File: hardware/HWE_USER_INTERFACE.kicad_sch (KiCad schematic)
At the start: 0 parts

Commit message: feat: Created Button I2C Interfaces
For now, all we are using is generic 1x5 Connectors following the DFR Robot's RGB Button pinout https://wiki.dfrobot.com/SKU_DFR0991_Gravity_I2C_RGB_LED_Button_Module#target_9
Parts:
- added J4: BTN_PLAY, symbol Connector_Generic:Conn_01x05
- added J5: BTN_REC, symbol Connector_Generic:Conn_01x05
- added J6: BTN_STOP, symbol Connector_Generic:Conn_01x05
- added J7: BTN_QUANTISE, symbol Connector_Generic:Conn_01x05
- added J8: BTN_OVERDUB, symbol Connector_Generic:Conn_01x05
- added J9: BTN_METRONOME, symbol Connector_Generic:Conn_01x05
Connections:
- new net +5V: J4.1 (Pin_1), J5.1 (Pin_1), J6.1 (Pin_1), J7.1 (Pin_1), J8.1 (Pin_1), J9.1 (Pin_1)
- new net BTN_METRONOME_INT: J9.5 (Pin_5)
- new net BTN_OVERDUB_INT: J8.5 (Pin_5)
- new net BTN_PLAY_INT: J4.5 (Pin_5)
- new net BTN_QUANTISE_INT: J7.5 (Pin_5)
- new net BTN_REC_INT: J5.5 (Pin_5)
- new net BTN_STOP_INT: J6.5 (Pin_5)
- new net GND: J4.2 (Pin_2), J5.2 (Pin_2), J6.2 (Pin_2), J7.2 (Pin_2), J8.2 (Pin_2), J9.2 (Pin_2)
- new net SCL: J4.3 (Pin_3)
- new net SDA: J4.4 (Pin_4), J5.4 (Pin_4), J6.4 (Pin_4), J7.4 (Pin_4), J8.4 (Pin_4), J9.4 (Pin_4)

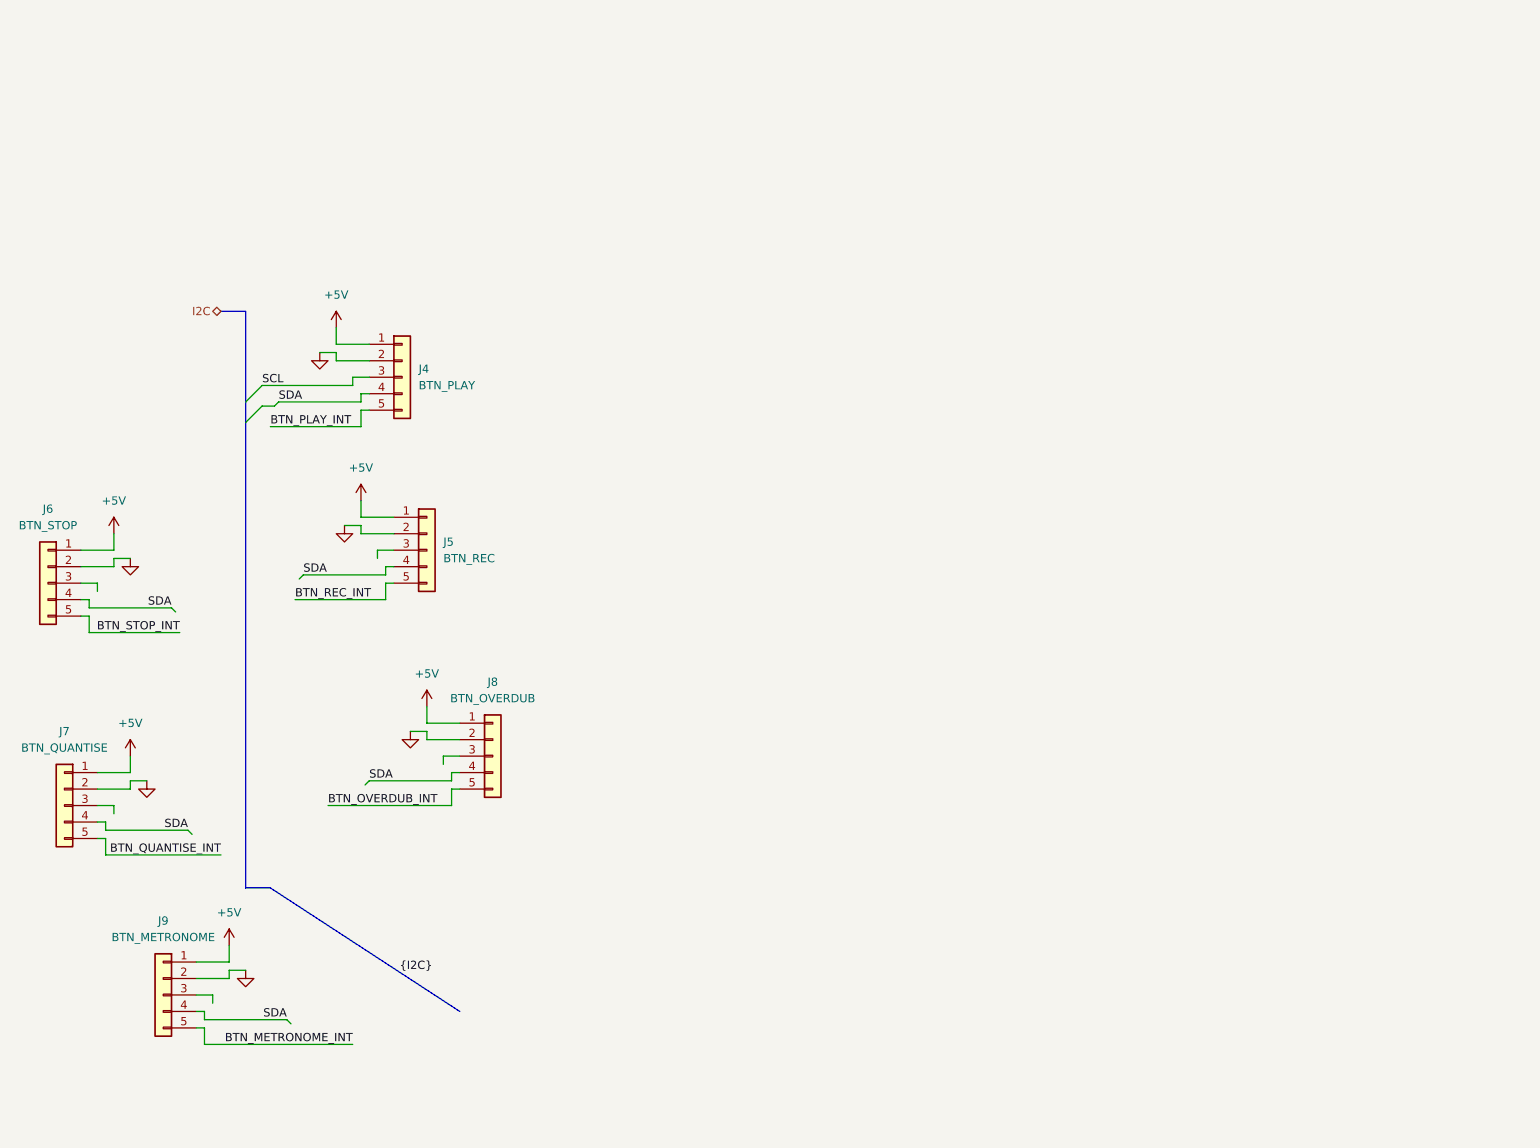
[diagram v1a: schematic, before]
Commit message: feat: Added Volume and Inf Scroll Encoders
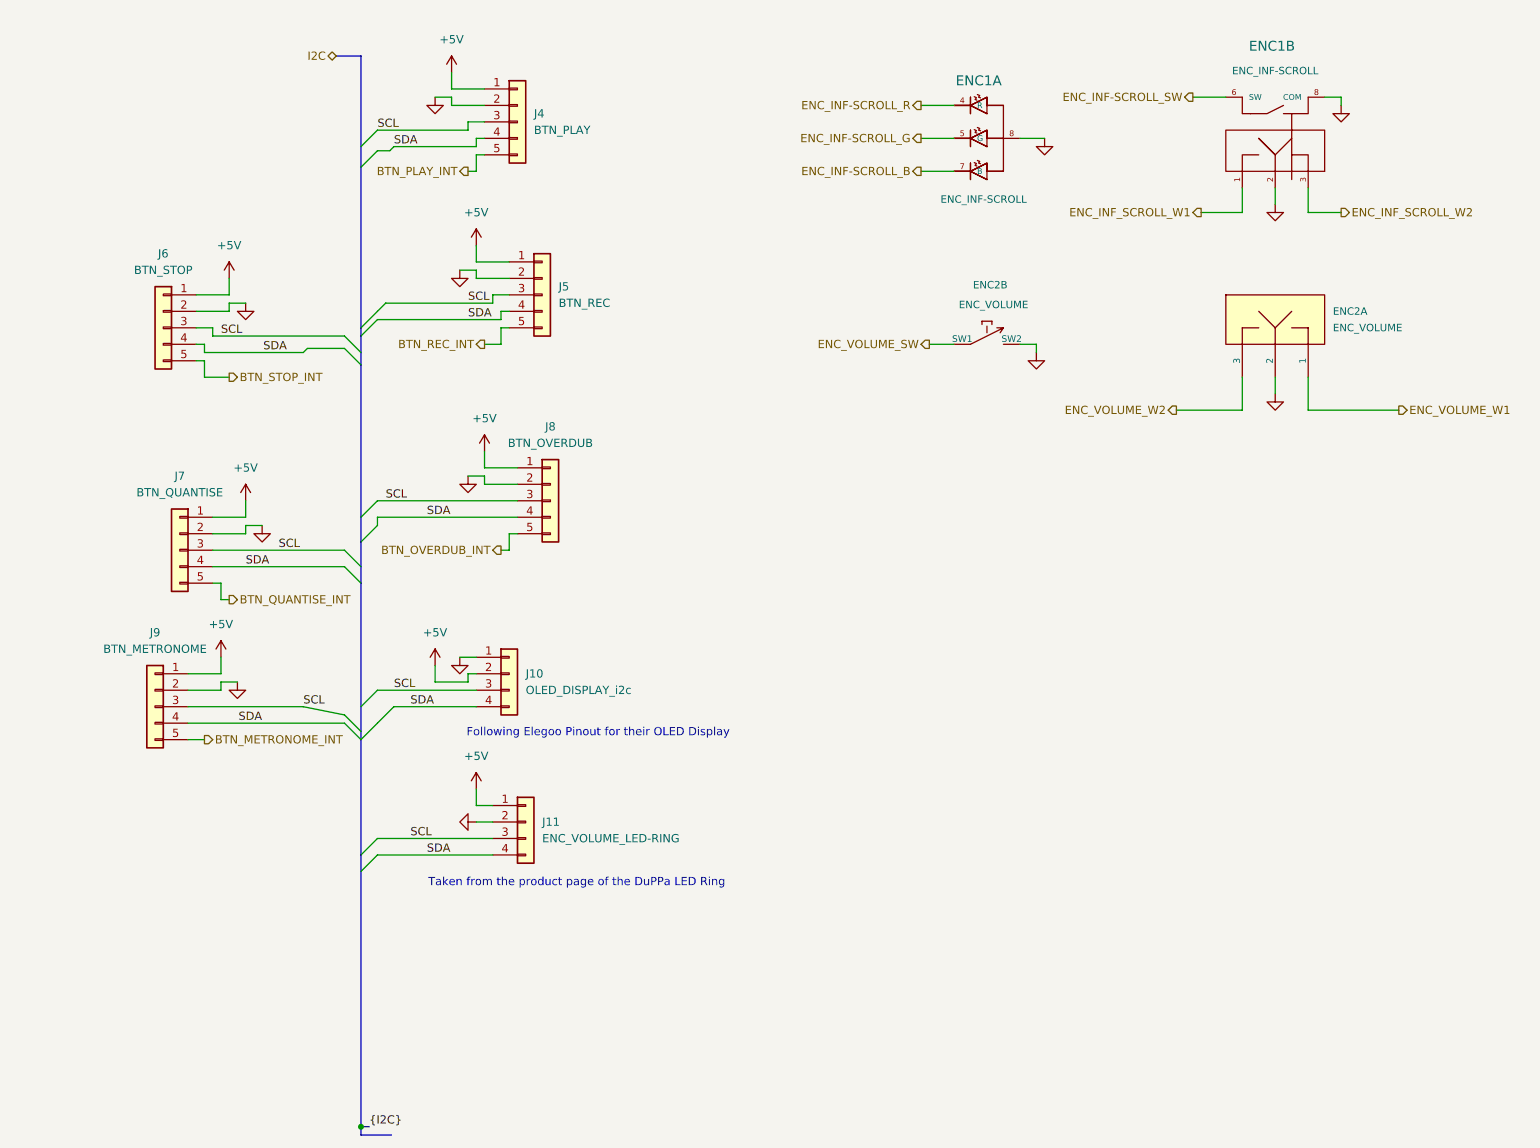
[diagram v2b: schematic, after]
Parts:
- added ENC1: ENC_INF-SCROLL, 4ms_Encoder:ENC_RGB_SPST_12mm, symbol 4ms_Switch:RGB_ROTARY_ENCODER-4ms-mech
- added ENC2: ENC_VOLUME, 4ms_Encoder:ENC_SPST_12mm, symbol 4ms_Switch:Encoder_Rotary_11mm_SPST_DShaft
- added J10: OLED_DISPLAY_i2c, symbol Connector_Generic:Conn_01x04
- added J11: ENC_VOLUME_LED-RING, symbol Connector_Generic:Conn_01x04
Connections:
- net +5V: now also J10.2 (Pin_2), J11.1 (Pin_1)
- net GND: now also ENC1.2, ENC1.8, ENC1.8 (COM), ENC2.2, ENC2.SW2, J10.1 (Pin_1), J11.2 (Pin_2)
- net SCL: now also J5.3 (Pin_3), J6.3 (Pin_3), J7.3 (Pin_3), J8.3 (Pin_3), J9.3 (Pin_3), J10.3 (Pin_3), J11.3 (Pin_3)
- net SDA: now also J10.4 (Pin_4), J11.4 (Pin_4)
- new net ENC_INF-SCROLL_B: ENC1.7 (B)
- new net ENC_INF-SCROLL_G: ENC1.5 (G)
- new net ENC_INF-SCROLL_R: ENC1.4 (R)
- new net ENC_INF-SCROLL_SW: ENC1.6 (SW)
- new net ENC_INF_SCROLL_W1: ENC1.1
- new net ENC_INF_SCROLL_W2: ENC1.3
- new net ENC_VOLUME_SW: ENC2.SW1
- new net ENC_VOLUME_W1: ENC2.1
- new net ENC_VOLUME_W2: ENC2.3
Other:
- note added: "Following Elegoo Pinout for their OLED Display"
- note added: "Taken from the product page of the DuPPa LED Ring"
- moved on the sheet: J4, J5, J6, J7, J8, J9

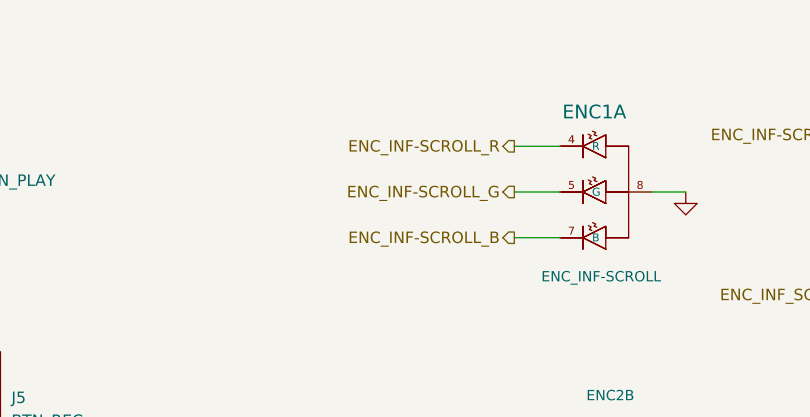
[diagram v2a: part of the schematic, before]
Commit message: feat: Connected main HW UI components to MCU
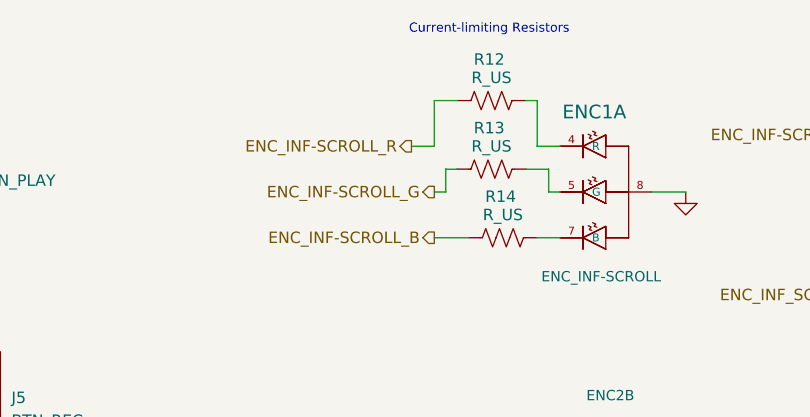
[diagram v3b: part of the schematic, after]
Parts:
- added R12, R13, R14: R_US, symbol Device:R_US
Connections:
- net ENC_INF-SCROLL_B: now also R14.1; no longer ENC1.7 (B)
- net ENC_INF-SCROLL_G: now also R13.1; no longer ENC1.5 (G)
- net ENC_INF-SCROLL_R: now also R12.1; no longer ENC1.4 (R)
- new net: ENC1.4 (R), R12.2
- new net: ENC1.5 (G), R13.2
- new net: ENC1.7 (B), R14.2
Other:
- note added: "Current-limiting Resistors"

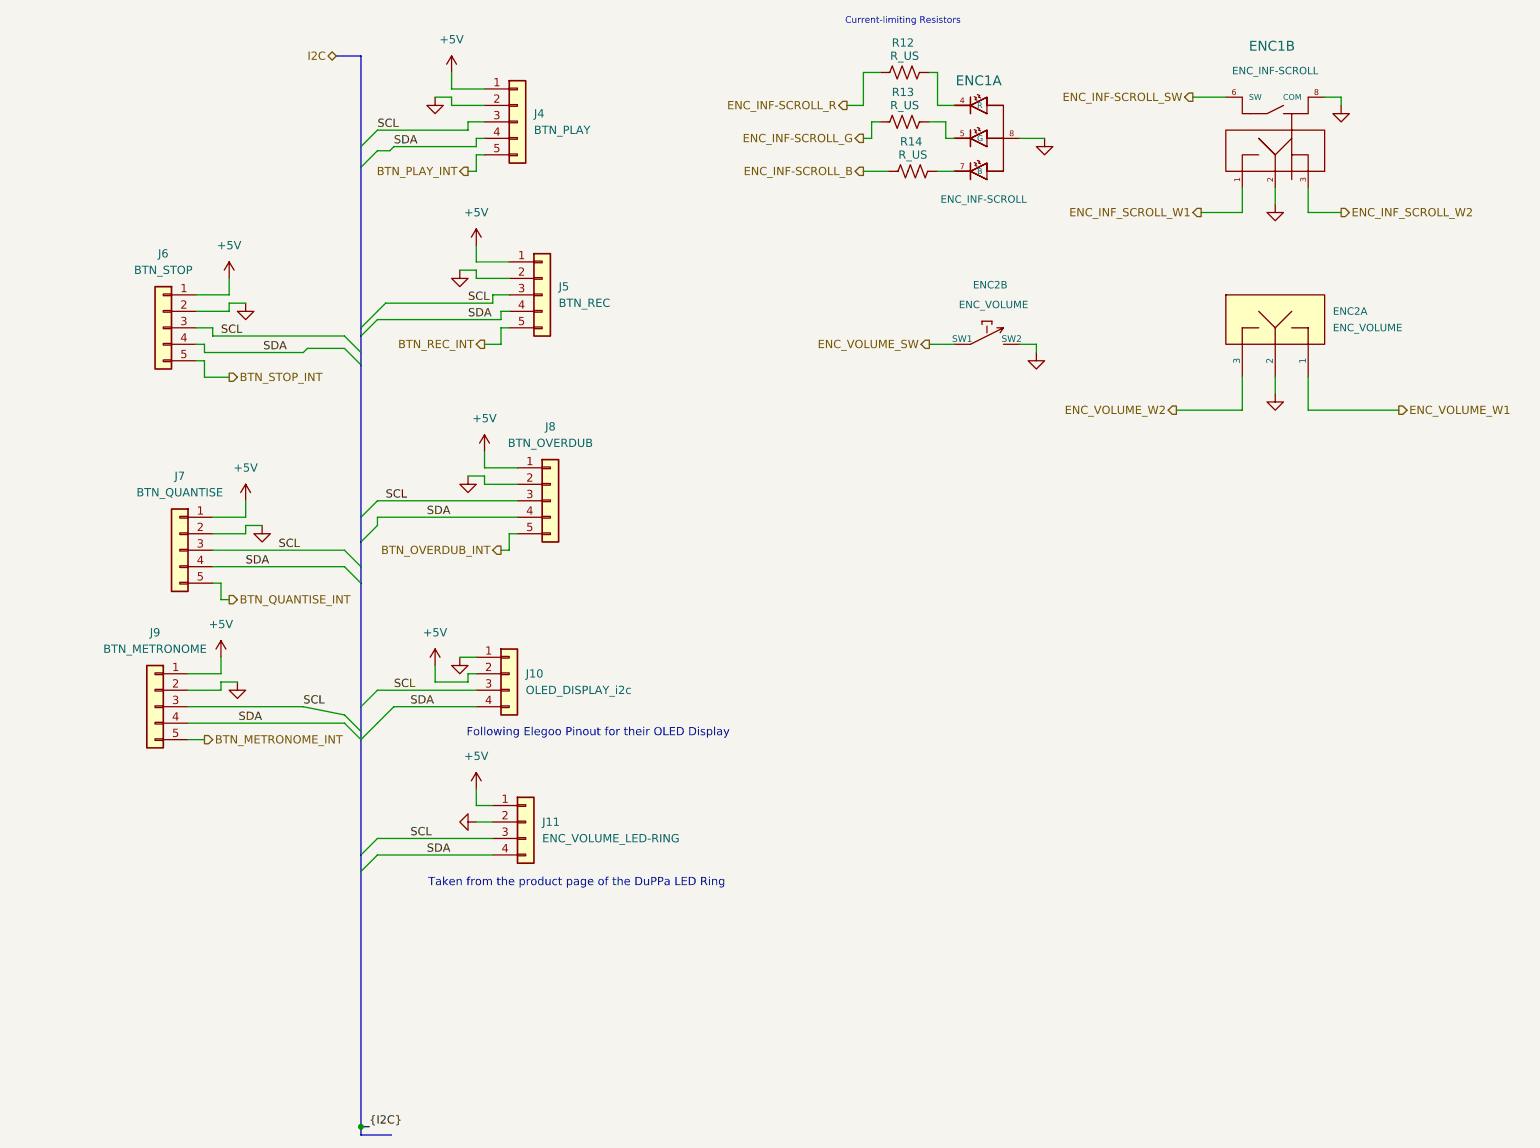
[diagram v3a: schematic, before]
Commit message: feat [HWE}; Added SPI Oled and refactor DuPPa LED
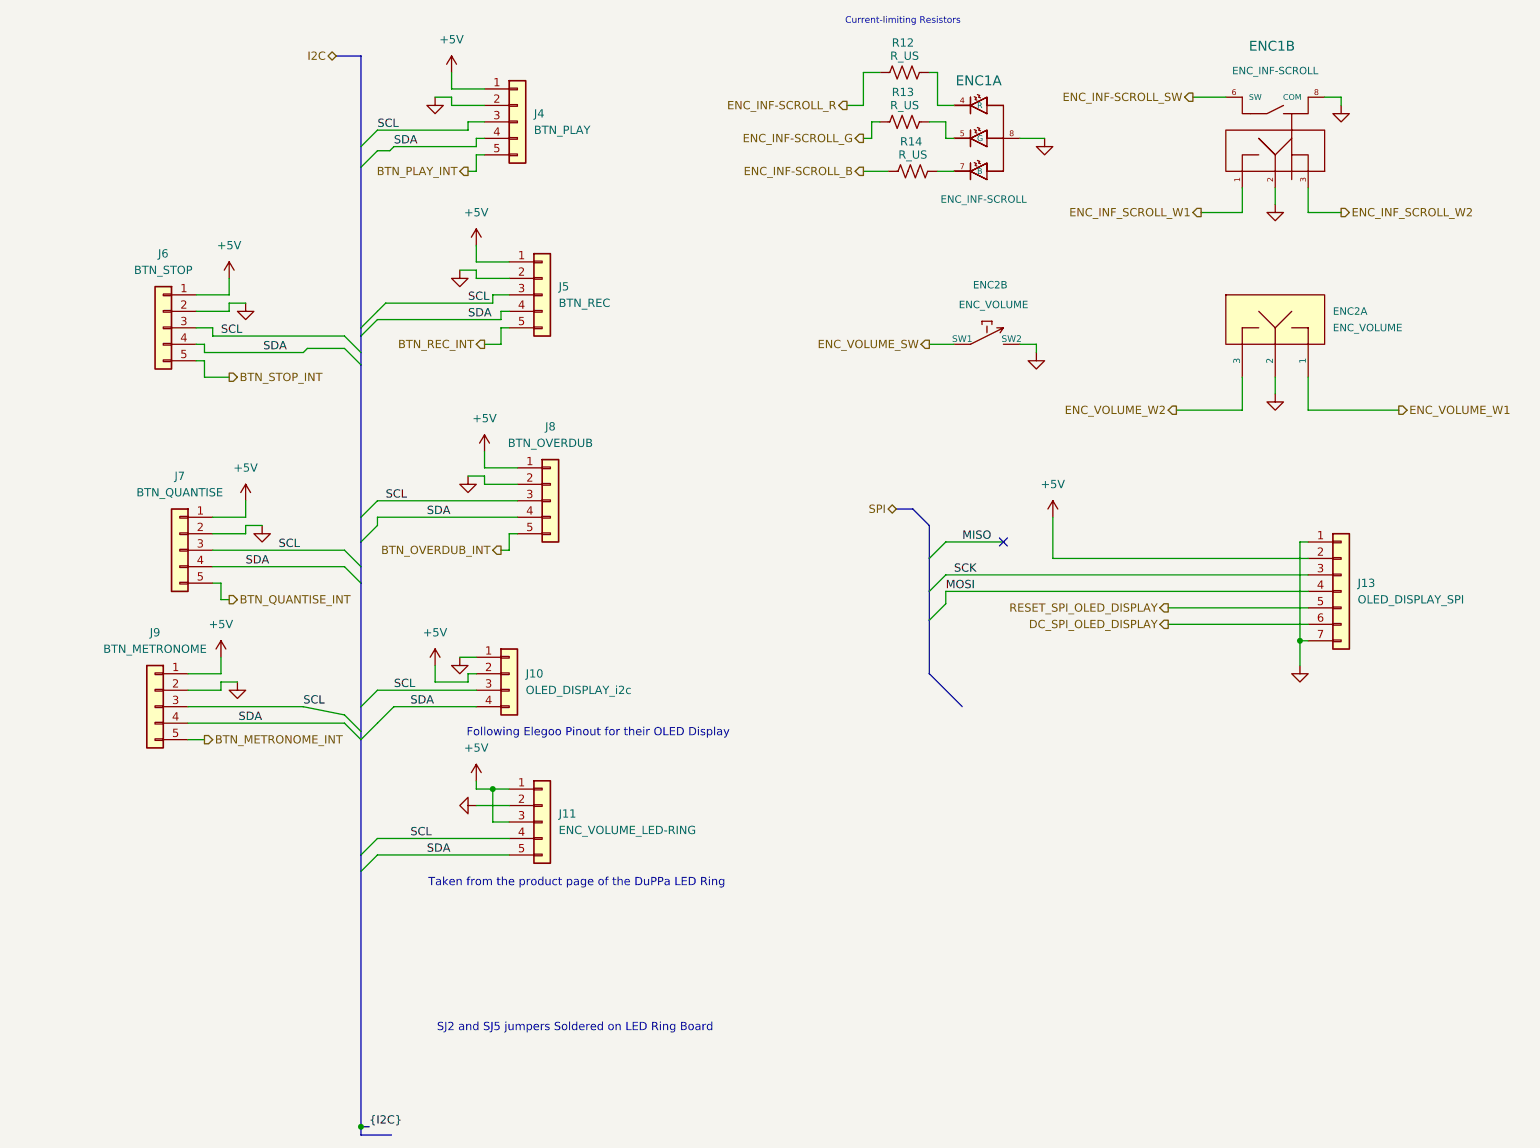
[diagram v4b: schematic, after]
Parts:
- added J13: OLED_DISPLAY_SPI, symbol Connector_Generic:Conn_01x07
- J11: symbol Connector_Generic:Conn_01x04 -> Connector_Generic:Conn_01x05
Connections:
- net +5V: now also J11.3 (Pin_3), J13.2 (Pin_2)
- net GND: now also J13.1 (Pin_1), J13.7 (Pin_7)
- net SCL: now also J11.4 (Pin_4); no longer J11.3 (Pin_3)
- net SDA: now also J11.5 (Pin_5); no longer J11.4 (Pin_4)
- new net DC_SPI_OLED_DISPLAY: J13.6 (Pin_6)
- new net MOSI: J13.4 (Pin_4)
- new net RESET_SPI_OLED_DISPLAY: J13.5 (Pin_5)
- new net SCK: J13.3 (Pin_3)
- no-connect marks 0 -> 1
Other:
- note added: "SJ2 and SJ5 jumpers Soldered on LED Ring Board"
